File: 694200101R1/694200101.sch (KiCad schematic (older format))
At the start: 249 parts, among them J1 USB4085-GF-A, J2 Conn_01x05_Male, J3 Conn_01x02_Male, SW1 MX_SW, SW10 MX_SW, SW100 MX_SW, SW101 MX_SW, SW102 MX_SW, SW103 MX_SW, SW104 MX_SW, SW105 MX_SW, SW106 MX_SW, SW107 MX_SW, SW11 MX_SW, SW12 MX_SW, SW13 MX_SW, SW14 MX_SW, SW15 MX_SW, SW16 MX_SW, SW17 MX_SW, SW18 MX_SW, SW19 MX_SW, SW2 MX_SW, SW20 MX_SW, SW21 MX_SW, SW22 MX_SW, SW23 MX_SW, SW24 MX_SW, SW25 MX_SW, SW26 MX_SW, SW27 MX_SW, SW28 MX_SW, SW29 MX_SW, SW3 MX_SW, SW30 MX_SW, SW31 MX_SW, SW32 MX_SW, SW33 MX_SW, SW34 MX_SW, SW35 MX_SW, SW36 MX_SW, SW37 MX_SW, SW38 MX_SW, SW39 MX_SW, SW4 MX_SW, SW40 MX_SW, SW41 MX_SW, SW42 MX_SW, SW43 MX_SW, SW44 MX_SW, SW45 MX_SW, SW46 MX_SW, SW47 MX_SW, SW48 MX_SW, SW49 MX_SW, SW5 MX_SW, SW50 MX_SW, SW51 MX_SW, SW52 MX_SW, SW53 MX_SW, SW54 MX_SW, SW55 MX_SW, SW56 MX_SW, SW57 MX_SW, SW58 MX_SW, SW59 MX_SW, SW6 MX_SW, SW60 MX_SW, SW61 MX_SW, SW62 MX_SW, SW63 MX_SW, SW64 MX_SW, SW65 MX_SW, SW66 MX_SW, SW67 MX_SW, SW68 MX_SW, SW69 MX_SW, SW7 MX_SW, SW70 MX_SW, SW71 MX_SW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

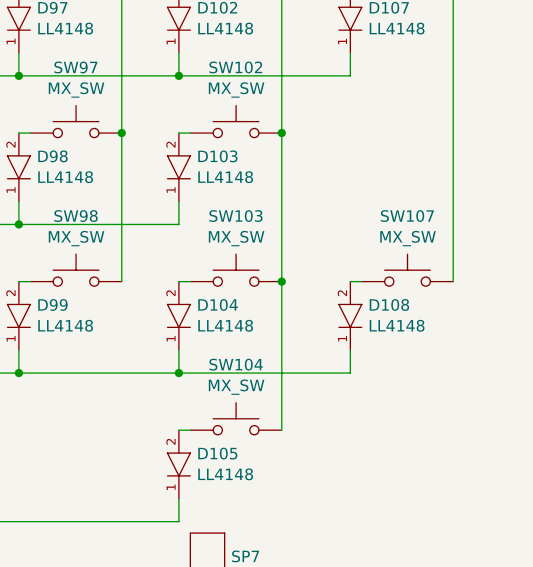
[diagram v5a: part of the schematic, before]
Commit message: allign more diodes, bottom half
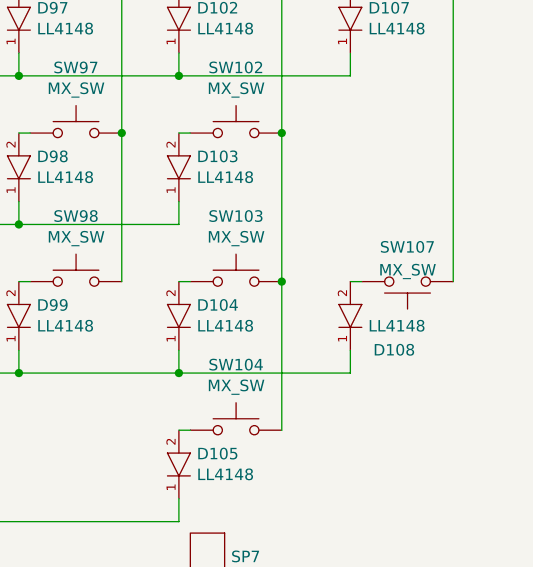
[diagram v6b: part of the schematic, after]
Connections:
- net COL_22: now also SW107.1; no longer SW107.2
- net at D108.2 (ANODE): now also SW107.2; no longer SW107.1
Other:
- moved on the sheet: SW107
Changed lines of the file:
@@
 U 1 1 637C9D8A
 P 15600 3400
-F 0 "D108" V 15804 3478 50  0000 L CNN
+F 0 "D108" V 16000 3500 50  0000 L CNN
 F 1 "LL4148" V 15895 3478 50  0000 L CNN
 F 2 "eec-fairchild:Fairchild_ON_Semiconductor-LL4148-0" H 15600 3800 50  0001 L CNN
@@
 U 1 1 637C9D77
 P 15850 3500
-F 0 "SW107" H 15850 3785 50  0000 C CNN
-F 1 "MX_SW" H 15850 3694 50  0000 C CNN
+F 0 "SW107" H 15850 3350 50  0000 C CNN
+F 1 "MX_SW" H 15850 3450 50  0000 C CNN
 F 2 "cldg:millmax-mxalps" H 15850 3700 50  0001 C CNN
 F 3 "~" H 15850 3700 50  0001 C CNN
 	1    15850 3500
-	1    0    0    -1
+	-1   0    0    1
 $EndComp
 Connection ~ 14850 2600

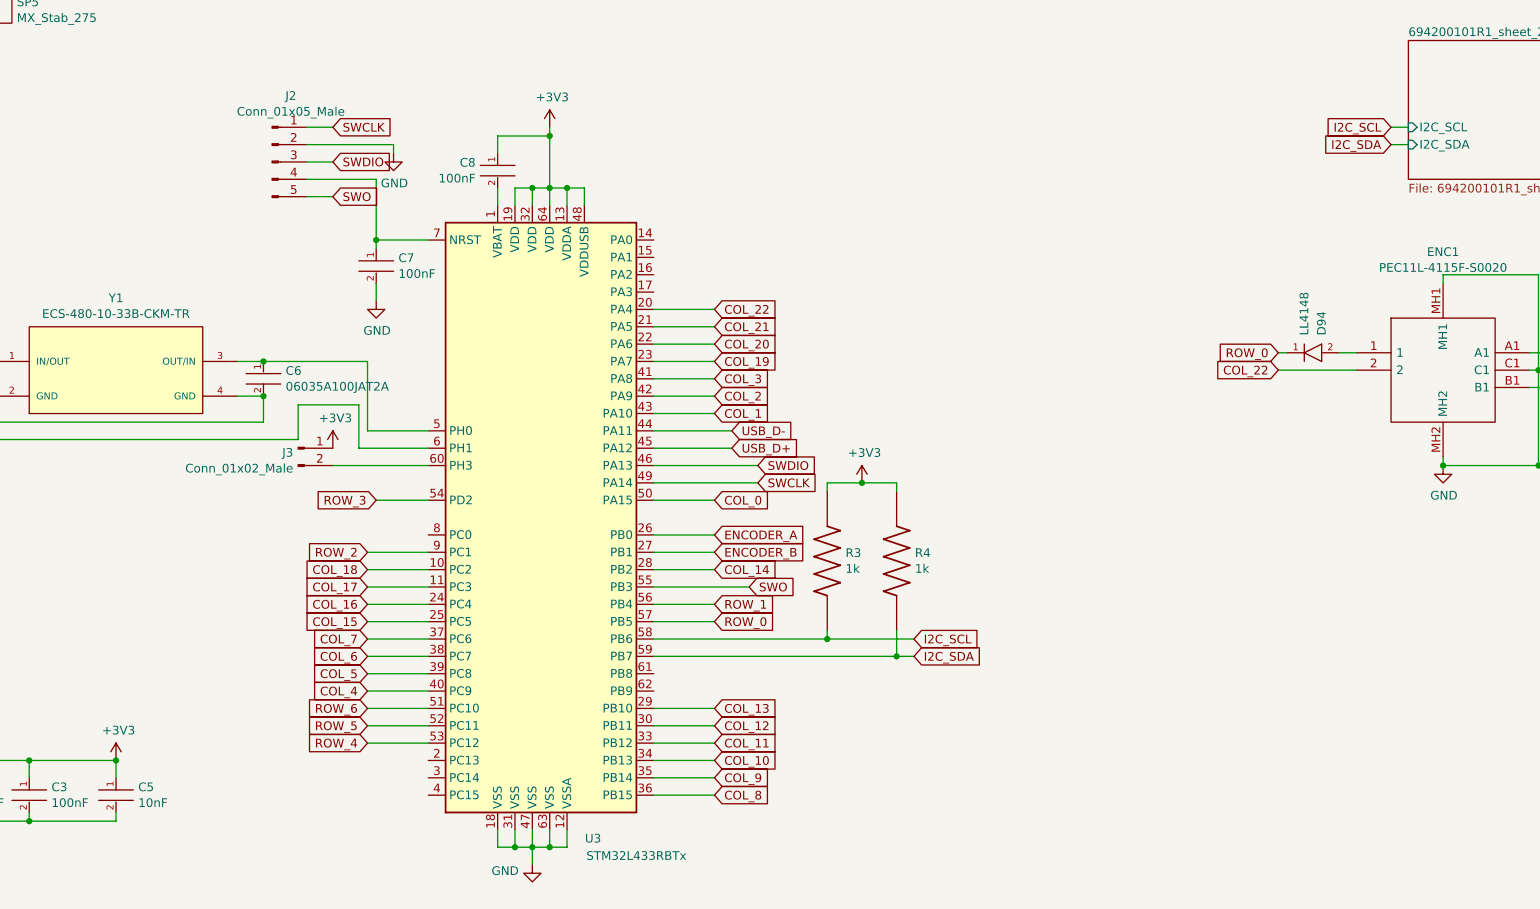
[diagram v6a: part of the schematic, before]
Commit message: Fixed Missing I2C Net
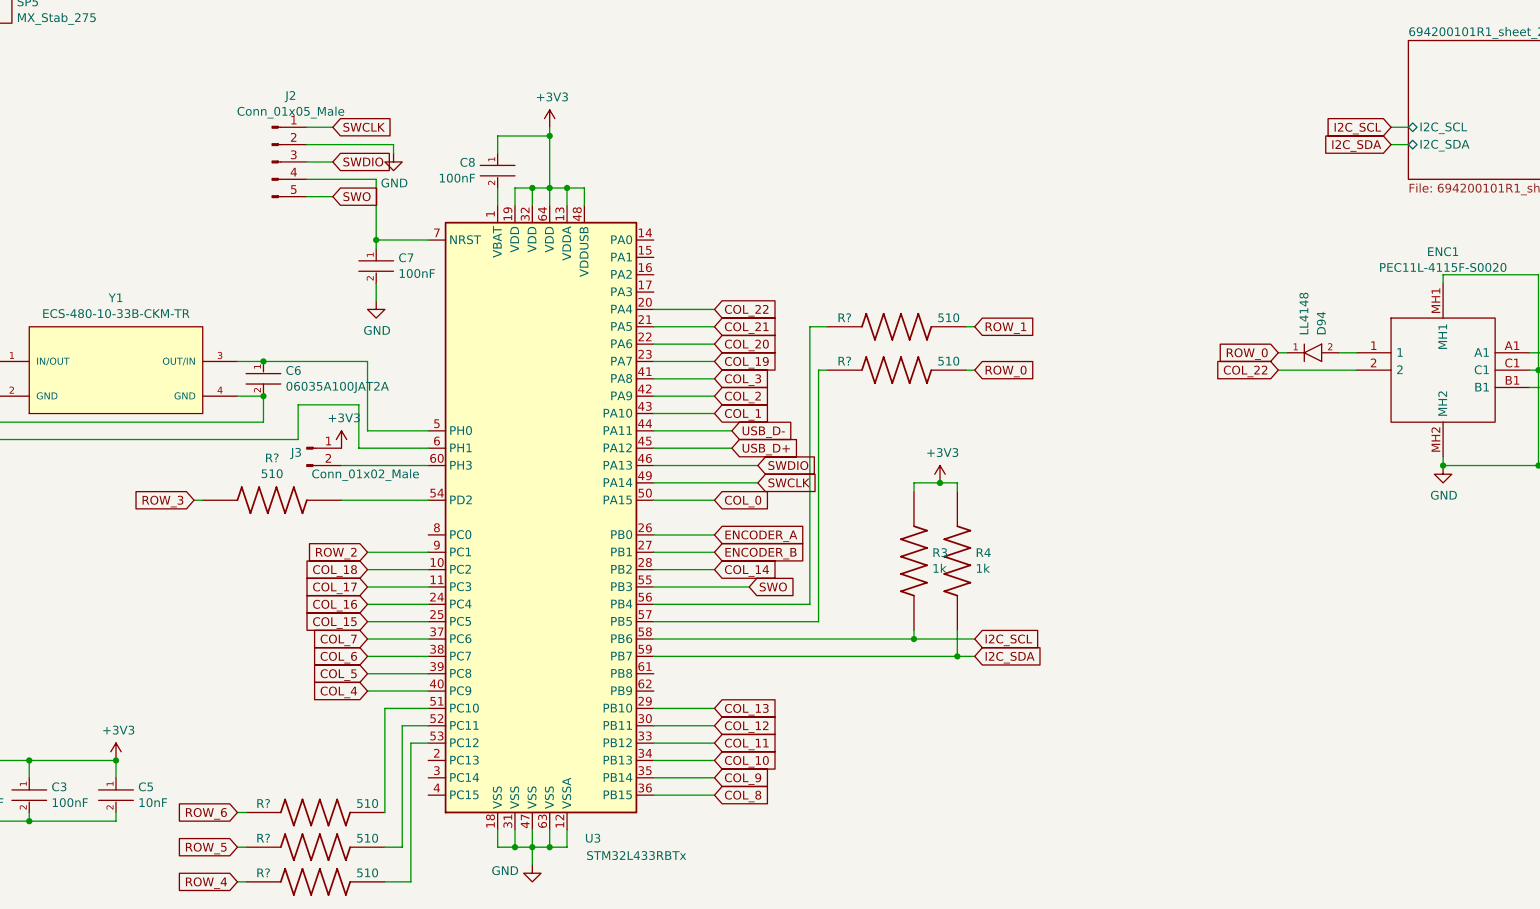
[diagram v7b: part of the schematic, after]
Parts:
- added R? (x6): RMCF0805FT510R, Resistor-Libs:RESC2012X65N, symbol Resistor-Lib:RMCF0805FT510R
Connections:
- net ROW_0: now also R?.2; no longer U3.57 (PB5)
- net ROW_1: now also R?.2; no longer U3.56 (PB4)
- net ROW_3: now also R?.1; no longer U3.54 (PD2)
- net ROW_4: now also R?.1; no longer U3.53 (PC12)
- net ROW_5: now also R?.1; no longer U3.52 (PC11)
- net ROW_6: now also R?.1; no longer U3.51 (PC10)
- new net: R?.2, U3.51 (PC10)
- new net: R?.2, U3.52 (PC11)
- new net: R?.2, U3.53 (PC12)
- new net: R?.2, U3.54 (PD2)
- new net: R?.1, U3.56 (PB4)
- new net: R?.1, U3.57 (PB5)
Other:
- moved on the sheet: J3, R3, R4
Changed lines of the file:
@@
 L Connector:Conn_01x02_Male J3
 U 1 1 6006B89E
-P 7500 7800
-F 0 "J3" H 7472 7774 50  0000 R CNN
-F 1 "Conn_01x02_Male" H 7472 7683 50  0000 R CNN
-F 2 "Connector_PinHeader_2.54mm:PinHeader_1x02_P2.54mm_Vertical" H 7500 7800 50  0001 C CNN
-F 3 "~" H 7500 7800 50  0001 C CNN
-	1    7500 7800
+P 7550 7800
+F 0 "J3" H 7522 7774 50  0000 R CNN
+F 1 "Conn_01x02_Male" H 8200 7650 50  0000 R CNN
+F 2 "Connector_PinHeader_2.54mm:PinHeader_1x02_P2.54mm_Vertical" H 7550 7800 50  0001 C CNN
+F 3 "~" H 7550 7800 50  0001 C CNN
+	1    7550 7800
 	1    0    0    -1
 $EndComp
@@
 L power:+3V3 #PWR010
 U 1 1 60076D41
-P 7700 7800
-F 0 "#PWR010" H 7700 7650 50  0001 C CNN
-F 1 "+3V3" H 7715 7973 50  0000 C CNN
-F 2 "" H 7700 7800 50  0001 C CNN
-F 3 "" H 7700 7800 50  0001 C CNN
-	1    7700 7800
+P 7750 7800
+F 0 "#PWR010" H 7750 7650 50  0001 C CNN
+F 1 "+3V3" H 7765 7973 50  0000 C CNN
+F 2 "" H 7750 7800 50  0001 C CNN
+F 3 "" H 7750 7800 50  0001 C CNN
+	1    7750 7800
 	1    0    0    -1
 $EndComp
@@
 $EndComp
 Wire Wire Line
-	7700 7900 8250 7900
+	7750 7900 8250 7900
 $Comp
 L capacitor-lib:CL10B104KB8NNNL C7
@@
 	0    1    1    0
 $EndComp
-Text GLabel 11050 8900 2    50   Input ~ 0
+Text GLabel 11400 8900 2    50   Input ~ 0
 I2C_SCL
-Text GLabel 11050 9000 2    50   Input ~ 0
+Text GLabel 11400 9000 2    50   Input ~ 0
 I2C_SDA
 Text GLabel 10000 7800 2    50   Input ~ 0
@@
 L Resistor-Lib:RMCF0603FT1K00 R3
 U 1 1 6001106E
-P 10550 8450
-F 0 "R3" V 10504 8555 50  0000 L CNN
-F 1 "RMCF0603FT1K00" V 10595 8555 50  0001 L CNN
-F 2 "Resistor-Libs:RESC1508X55N" H 10550 8450 50  0001 L BNN
-F 3 "" H 10550 8450 50  0001 L BNN
-F 4 "1k" V 10595 8555 50  0000 L CNN "resistance"
-	1    10550 8450
+P 11050 8450
+F 0 "R3" V 11004 8555 50  0000 L CNN
+F 1 "RMCF0603FT1K00" V 11095 8555 50  0001 L CNN
+F 2 "Resistor-Libs:RESC1508X55N" H 11050 8450 50  0001 L BNN
+F 3 "" H 11050 8450 50  0001 L BNN
+F 4 "1k" V 11095 8555 50  0000 L CNN "resistance"
+	1    11050 8450
 	0    1    1    0
 $EndComp
@@
 L Resistor-Lib:RMCF0603FT1K00 R4
 U 1 1 60013A68
-P 10950 8450
-F 0 "R4" V 10904 8555 50  0000 L CNN
-F 1 "RMCF0603FT1K00" V 10995 8555 50  0001 L CNN
-F 2 "Resistor-Libs:RESC1508X55N" H 10950 8450 50  0001 L BNN
-F 3 "" H 10950 8450 50  0001 L BNN
-F 4 "1k" V 10995 8555 50  0000 L CNN "resistance"
-	1    10950 8450
+P 11300 8450
+F 0 "R4" V 11254 8555 50  0000 L CNN
+F 1 "RMCF0603FT1K00" V 11345 8555 50  0001 L CNN
+F 2 "Resistor-Libs:RESC1508X55N" H 11300 8450 50  0001 L BNN
+F 3 "" H 11300 8450 50  0001 L BNN
+F 4 "1k" V 11345 8555 50  0000 L CNN "resistance"
+	1    11300 8450
 	0    1    1    0
 $EndComp
 Wire Wire Line
-	10550 8850 10550 8900
-Connection ~ 10550 8900
+	11050 8850 11050 8900
+Connection ~ 11050 8900
 Wire Wire Line
-	10550 8900 11050 8900
+	11050 8900 11400 8900
 Wire Wire Line
-	10950 8850 10950 9000
-Connection ~ 10950 9000
+	11300 8850 11300 9000
+Connection ~ 11300 9000
 Wire Wire Line
-	10950 9000 11050 9000
+	11300 9000 11400 9000
 Wire Wire Line
-	10550 8050 10550 8000
+	11050 8050 11050 8000
 Wire Wire Line
-	10550 8000 10750 8000
+	11050 8000 11200 8000
 Wire Wire Line
-	10950 8000 10950 8050
+	11300 8000 11300 8050
 $Comp
 L power:+3V3 #PWR013
 U 1 1 60025E0E
-P 10750 8000
-F 0 "#PWR013" H 10750 7850 50  0001 C CNN
-F 1 "+3V3" H 10765 8173 50  0000 C CNN
-F 2 "" H 10750 8000 50  0001 C CNN
-F 3 "" H 10750 8000 50  0001 C CNN
-	1    10750 8000
+P 11200 8000
+F 0 "#PWR013" H 11200 7850 50  0001 C CNN
+F 1 "+3V3" H 11215 8173 50  0000 C CNN
+F 2 "" H 11200 8000 50  0001 C CNN
+F 3 "" H 11200 8000 50  0001 C CNN
+	1    11200 8000
 	1    0    0    -1
 $EndComp
-Connection ~ 10750 8000
+Connection ~ 11200 8000
 Wire Wire Line
-	10750 8000 10950 8000
-Text GLabel 9900 8800 2    50   Input ~ 0
+	11200 8000 11300 8000
+Text GLabel 11400 7350 2    50   Input ~ 0
 ROW_0
-Text GLabel 9900 8700 2    50   Input ~ 0
+Text GLabel 11400 7100 2    50   Input ~ 0
 ROW_1
 Text GLabel 7900 8400 0    50   Input ~ 0
 ROW_2
 Wire Wire Line
-	8250 8100 7950 8100
-Text GLabel 7950 8100 0    50   Input ~ 0
+	8250 8100 7750 8100
+Text GLabel 6900 8100 0    50   Input ~ 0
 ROW_3
-Wire Wire Line
-	8250 9500 7900 9500
-Text GLabel 7900 9500 0    50   Input ~ 0
+Text GLabel 7150 10300 0    50   Input ~ 0
 ROW_4
 Wire Wire Line
-	8250 9400 7900 9400
-Text GLabel 7900 9400 0    50   Input ~ 0
+	8250 9400 8100 9400
+Text GLabel 7150 10100 0    50   Input ~ 0
 ROW_5
 Wire Wire Line
-	8250 9300 7900 9300
-Text GLabel 7900 9300 0    50   Input ~ 0
+	8250 9300 8000 9300
+Text GLabel 7150 9900 0    50   Input ~ 0
 ROW_6
 Text GLabel 9900 8100 2    50   Input ~ 0
@@
 F0 "694200101R1_sheet_2" 50
 F1 "694200101R1_sheet_2.sch" 50
-F2 "I2C_SDA" I L 13900 6050 50
-F3 "I2C_SCL" I L 13900 5950 50
+F2 "I2C_SDA" B L 13900 6050 50
+F3 "I2C_SCL" B L 13900 5950 50
 $EndSheet
 Wire Wire Line
@@
 $EndComp
 Wire Wire Line
-	9550 9000 10950 9000
-Wire Wire Line
-	9550 8900 10550 8900
+	9550 9000 11300 9000
 Wire Wire Line
-	9550 8800 9900 8800
-Wire Wire Line
-	9550 8700 9900 8700
+	9550 8900 11050 8900
 Wire Wire Line
 	9550 8500 9900 8500
@@
 	9550 7300 9900 7300
 Wire Wire Line
-	9550 7200 9900 7200
-Wire Wire Line
-	9550 7100 9900 7100
-Wire Wire Line
-	9550 7000 9900 7000
-Wire Wire Line
 	9550 8100 9900 8100
 Wire Wire Line
@@
 	0    1    1    0
 $EndComp
+Wire Wire Line
+	9550 7000 9900 7000
+Wire Wire Line
+	9550 7100 9900 7100
+Wire Wire Line
+	9550 7200 9900 7200
+Wire Wire Line
+	10450 8700 10450 7100
+Wire Wire Line
+	9550 8700 10450 8700
+Wire Wire Line
+	10500 8800 10500 7350
+Wire Wire Line
+	10500 7350 10550 7350
+Wire Wire Line
+	9550 8800 10500 8800
+Wire Wire Line
+	10450 7100 10550 7100
+$Comp
+L Resistor-Lib:RMCF0805FT510R R?
+U 1 1 61756588
+P 10950 7100
+F 0 "R?" H 10650 7150 50  0000 C CNN
+F 1 "RMCF0805FT510R" H 10650 6850 50  0001 L BNN
+F 2 "Resistor-Libs:RESC2012X65N" H 10650 6950 50  0001 L BNN
+F 3 "" H 10950 7100 50  0001 L BNN
+F 4 "510" H 11250 7150 50  0000 C CNN "reistance"
+	1    10950 7100
+	1    0    0    -1
+$EndComp
+Wire Wire Line
+	11350 7100 11400 7100
+Wire Wire Line
+	11400 7350 11350 7350
+$Comp
+L Resistor-Lib:RMCF0805FT510R R?
+U 1 1 6183038F
+P 10950 7350
+F 0 "R?" H 10650 7400 50  0000 C CNN
+F 1 "RMCF0805FT510R" H 10650 7100 50  0001 L BNN
+F 2 "Resistor-Libs:RESC2012X65N" H 10650 7200 50  0001 L BNN
+F 3 "" H 10950 7350 50  0001 L BNN
+F 4 "510" H 11250 7400 50  0000 C CNN "reistance"
+	1    10950 7350
+	1    0    0    -1
+$EndComp
+$Comp
+L Resistor-Lib:RMCF0805FT510R R?
+U 1 1 61907867
+P 7350 8100
+F 0 "R?" H 7350 8342 50  0000 C CNN
+F 1 "RMCF0805FT510R" H 7050 7850 50  0001 L BNN
+F 2 "Resistor-Libs:RESC2012X65N" H 7050 7950 50  0001 L BNN
+F 3 "" H 7350 8100 50  0001 L BNN
+F 4 "510" H 7350 8251 50  0000 C CNN "reistance"
+	1    7350 8100
+	1    0    0    -1
+$EndComp
+Wire Wire Line
+	6900 8100 6950 8100
+Wire Wire Line
+	8150 9500 8250 9500
+Wire Wire Line
+	8150 9500 8150 10300
+Wire Wire Line
+	8150 10300 8000 10300
+$Comp
+L Resistor-Lib:RMCF0805FT510R R?
+U 1 1 61BF657B
+P 7600 10300
+F 0 "R?" H 7300 10350 50  0000 C CNN
+F 1 "RMCF0805FT510R" H 7300 10050 50  0001 L BNN
+F 2 "Resistor-Libs:RESC2012X65N" H 7300 10150 50  0001 L BNN
+F 3 "" H 7600 10300 50  0001 L BNN
+F 4 "510" H 7900 10350 50  0000 C CNN "reistance"
+	1    7600 10300
+	1    0    0    -1
+$EndComp
+Wire Wire Line
+	7150 10300 7200 10300
+$Comp
+L Resistor-Lib:RMCF0805FT510R R?
+U 1 1 61C65077
+P 7600 10100
+F 0 "R?" H 7300 10150 50  0000 C CNN
+F 1 "RMCF0805FT510R" H 7300 9850 50  0001 L BNN
+F 2 "Resistor-Libs:RESC2012X65N" H 7300 9950 50  0001 L BNN
+F 3 "" H 7600 10100 50  0001 L BNN
+F 4 "510" H 7900 10150 50  0000 C CNN "reistance"
+	1    7600 10100
+	1    0    0    -1
+$EndComp
+Wire Wire Line
+	7150 10100 7200 10100
+Wire Wire Line
+	7150 9900 7200 9900
+Wire Wire Line
+	8100 9400 8100 10100
+Wire Wire Line
+	8100 10100 8000 10100
+Wire Wire Line
+	8000 9300 8000 9900
+$Comp
+L Resistor-Lib:RMCF0805FT510R R?
+U 1 1 61E7DED3
+P 7600 9900
+F 0 "R?" H 7300 9950 50  0000 C CNN
+F 1 "RMCF0805FT510R" H 7300 9650 50  0001 L BNN
+F 2 "Resistor-Libs:RESC2012X65N" H 7300 9750 50  0001 L BNN
+F 3 "" H 7600 9900 50  0001 L BNN
+F 4 "510" H 7900 9950 50  0000 C CNN "reistance"
+	1    7600 9900
+	1    0    0    -1
+$EndComp
 $EndSCHEMATC
